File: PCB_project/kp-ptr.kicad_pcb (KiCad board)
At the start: 4 copper layers, 26 x 56 mm, 111 parts, among them J1 ESP32_PROG_CON, J10 Conn_01x02, J11 Conn_01x02, J4 USB_C_Receptacle_USB2.0, Q1 AO3400A, Q2 AO3401A, Q4 AO3401A, Q5 AO3401A, Q6 AO3400A, Q7 AO3400A, SW1 JS202011CQN, U1 ESP32-C3FH4, U11 USBLC6-2SC6-ES, U3 BMP581, U4 LSM6DSV32, U5 SPX3819M5-L-3-3, U6 TP4054-42, Y2 XRCGB40M000F4M00R0

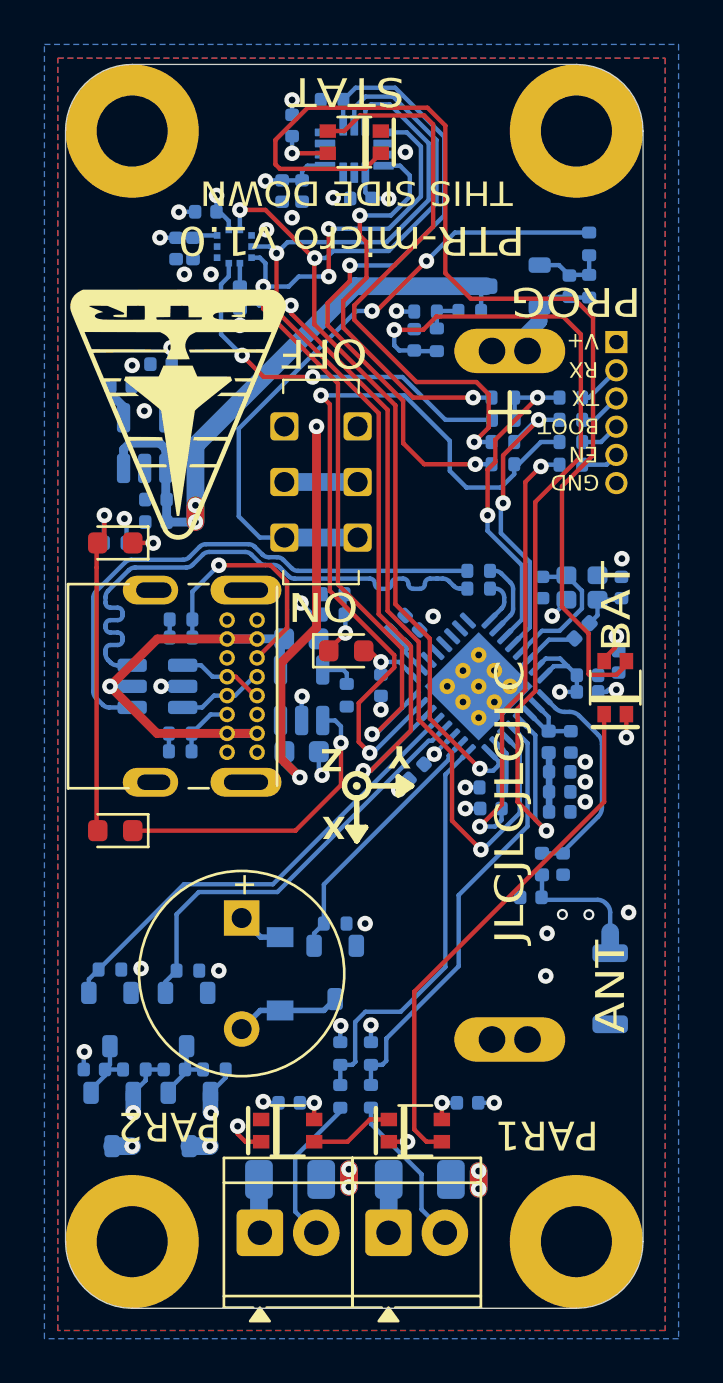
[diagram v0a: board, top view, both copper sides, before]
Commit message: Almost ready version. Require more GND vias etc
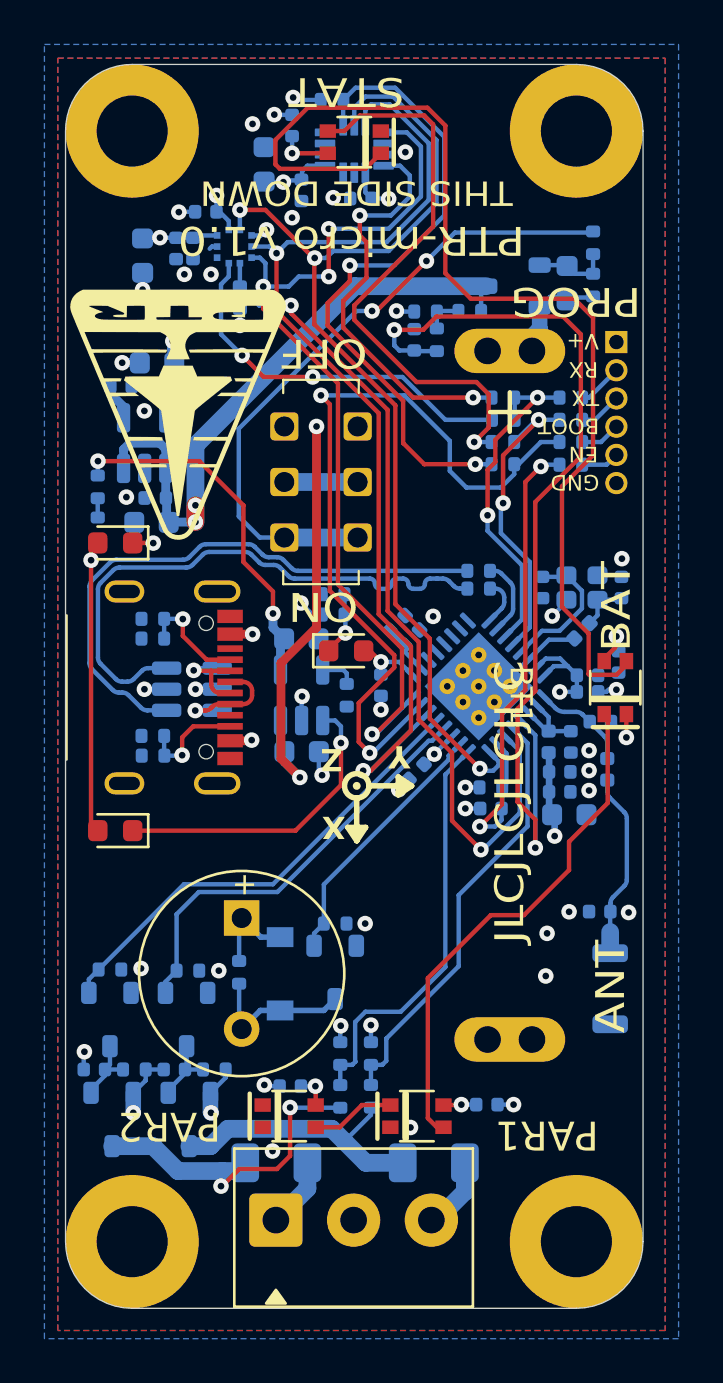
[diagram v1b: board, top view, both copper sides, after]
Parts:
- removed J10, J11: Conn_01x02, TerminalBlock_TE-Connectivity:TerminalBlock_TE_282834-2_1x02_P2.54mm_Horizontal
- removed J4: USB_C_Receptacle_USB2.0, KP-PTR_lib:USB_C_213716
- added C26: 10uF, Capacitor_SMD:C_0603_1608Metric, B.Cu at (0.47, 5.61)
- added J3: DB125-3.5-3P-GN-S, TerminalBlock_Phoenix:TerminalBlock_Phoenix_PT-1,5-3-3.5-H_1x03_P3.50mm_Horizontal, F.Cu at (6.47, 49.0)
- added R36: 1k, Resistor_SMD:R_0402_1005Metric, B.Cu at (-1.55, 16.0)
- added R44: 1k, Resistor_SMD:R_0402_1005Metric, B.Cu at (4.82, 37.9)
- added U2: USB4105-GF-A-12, KP-PTR_lib:USB_C_16P_SMD_USB4105-GF-A, F.Cu at (3.83, 25.1)
- C10, C9: value 12p -> 12pF
- C11, C13, C6: value 1u -> 1uF
- C12, C14, C15, C3, C7, C8: value 100n -> 100nF
- C21, C44, C57, C68: footprint Capacitor_SMD:C_0402_1005Metric -> Capacitor_SMD:C_0603_1608Metric
- C5: value 10u -> 10uF; footprint Capacitor_SMD:C_0402_1005Metric -> Capacitor_SMD:C_0603_1608Metric
- LS1: value CBT-09427-SMT -> GMD0955YB-3V2700
- R35: value 2k2 -> 1k
- moved C2 6.63 mm to (21.1, 26.6), turned to 0 degrees
- moved L1 5.18 mm to (21.4, 28.7)
- moved C1 3.17 mm to (21.1, 35.1)
- moved C21 2.09 mm to (5.94, 1.50), turned to 90 degrees
- moved U11 1.56 mm to (2.69, 25.1)
- moved R81 1.27 mm to (0.93, 22.9)
- moved R84 1.27 mm to (0.93, 22.0)
- moved R83 1.24 mm to (0.94, 28.1)
- moved R82 1.24 mm to (0.93, 27.2)
- moved R35 1.01 mm to (-1.55, 17.9), turned to 90 degrees
- moved F3 0.98 mm to (13.6, 46.5)
- moved F2 0.97 mm to (6.49, 46.5), turned to 180 degrees
- moved C20 0.87 mm to (16.0, 43.8)
- moved C22 0.87 mm to (7.62, 2.67)
- moved C24 0.75 mm to (7.12, 43.0)
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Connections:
- F2 pad 2: Earth -> Net-(Q2-D)
- F3 pad 1: Net-(J11-Pin_1) -> Net-(Q4-D)
- F3 pad 2: Earth -> Net-(J3-Pin_3)
- Q2 pad 3: Net-(J10-Pin_2) -> Net-(Q2-D)
- Q4 pad 3: Net-(J11-Pin_2) -> Net-(Q4-D)
- R35 pad 2: VBUS -> Net-(R35-Pad2)
- R61 pad 2: Net-(J10-Pin_2) -> Net-(Q2-D)
- R62 pad 2: Net-(J11-Pin_2) -> Net-(Q4-D)
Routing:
- net Net-(J11-Pin_2): track 21.0 -> 0.00 mm, vias 1 -> 0
- net Net-(J10-Pin_2): track 18.5 -> 0.00 mm, vias 1 -> 0
- net Net-(Q2-D): track 0.00 -> 15.7 mm, vias 0 -> 2
- net Net-(Q4-D): track 0.00 -> 12.6 mm
- net VBUS: track 30.4 -> 38.0 mm, vias 2 -> 5
- net Earth: track 26.4 -> 20.0 mm, vias 45 -> 43
- net Net-(U2-CC1): track 11.1 -> 5.06 mm
- net Net-(U1-LNA_IN): track 10.1 -> 4.42 mm
- net +3V3: track 36.8 -> 41.8 mm, vias 14 -> 16
- net Net-(J3-Pin_3): track 0.00 -> 4.83 mm
- net VCC: track 70.0 -> 73.1 mm
- net Net-(J11-Pin_1): track 2.40 -> 0.00 mm
- net Net-(U2-CC2): track 2.76 -> 4.86 mm, vias 0 -> 1
- net Net-(D14-A): track 4.77 -> 6.86 mm
- net Net-(AE1-FEED): track 6.31 -> 8.35 mm
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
